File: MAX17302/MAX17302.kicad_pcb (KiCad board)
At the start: 2 copper layers, 20.4 x 50.6 mm, 12 parts, among them J1 Conn_01x02, J2 Conn_01x02, J3 Conn_01x03, Q1 Q_NMOS_DSG, Q2 Q_NMOS_DSG, U1 MAX17302G+T

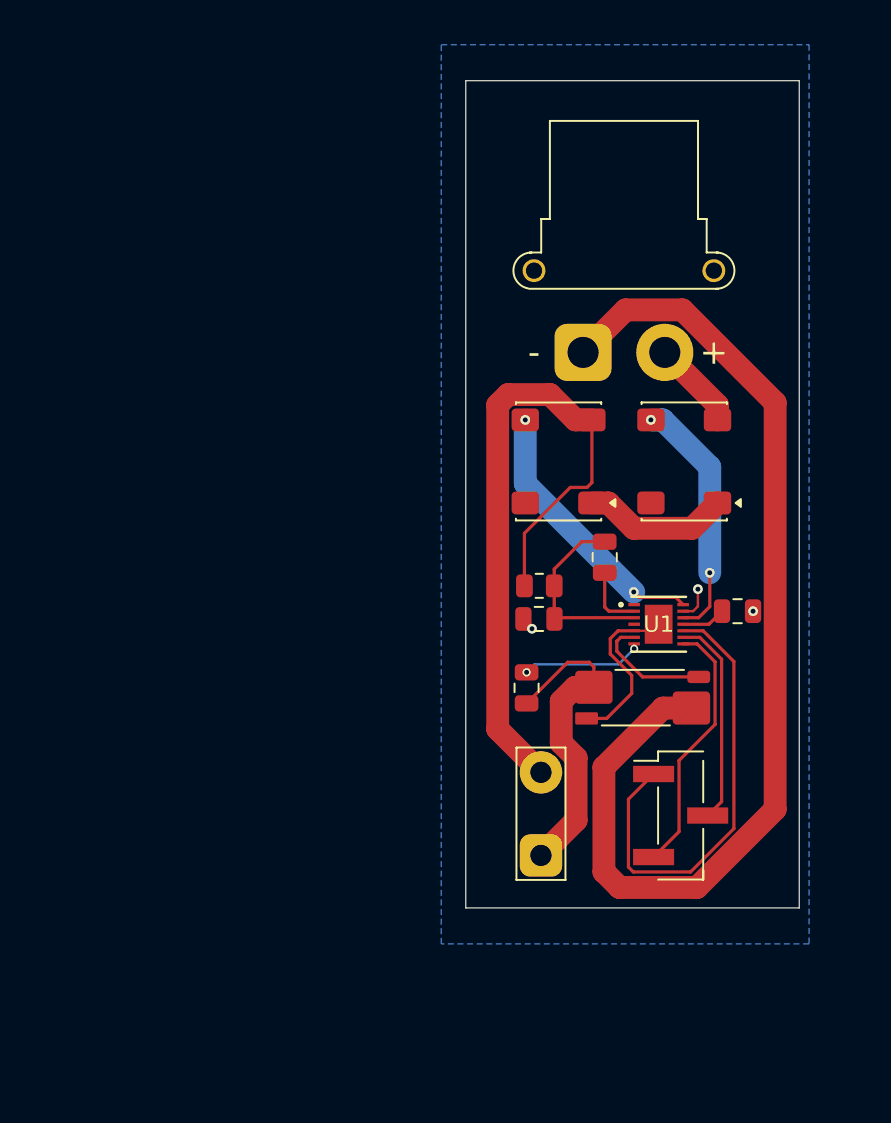
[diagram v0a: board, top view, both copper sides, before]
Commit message: Update PCB layout and add NTC thermistor
- Resolved clearance issues to ensure design safety.
- Adjusted trace widths for better routing.
- Optimized component placements and overall layout.
- Added NTC thermistor for temperature monitoring.
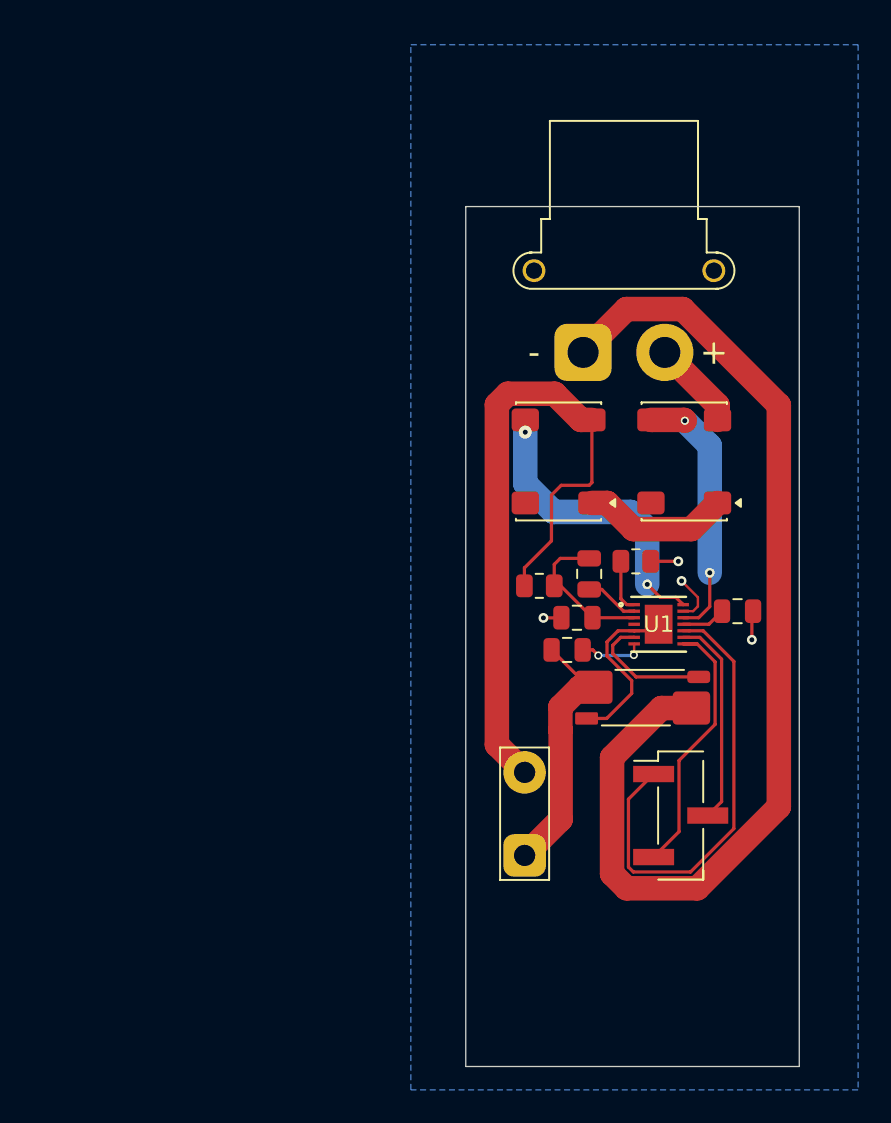
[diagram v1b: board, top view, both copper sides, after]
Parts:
- added TH1: 10kΩ, Resistor_SMD:R_0805_2012Metric, F.Cu at (149.4, 96.6)
- moved C2 3.40 mm to (145.2, 102.0), turned to 180 degrees
- moved C3 2.33 mm to (145.8, 100.0)
- moved C1 1.39 mm to (146.6, 97.4)
- moved J2 1.00 mm to (142.6, 114.6)
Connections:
- U1 pad 1: unconnected-(U1-TH-Pad1) -> Net-(U1-TH)
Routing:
- net GND: track 2.08 -> 7.57 mm, vias 3 -> 4
- net Net-(U1-REG): track 7.48 -> 3.56 mm
- net /CELL-: track 19.6 -> 16.2 mm
- net Net-(U1-TH): track 0.00 -> 3.25 mm
- net /BATT: track 11.7 -> 9.70 mm
- net /CHG: track 16.6 -> 18.0 mm
- net /DIS: track 15.2 -> 16.1 mm
- net Net-(J3-Pin_3): track 15.9 -> 16.7 mm
- net Net-(U1-CP): track 4.00 -> 3.30 mm
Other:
- board size 20.4 x 50.6 mm -> 20.4 x 52.6 mm

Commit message: Rebuild the MAX17302 PCB
also add new 3D of MAX17302
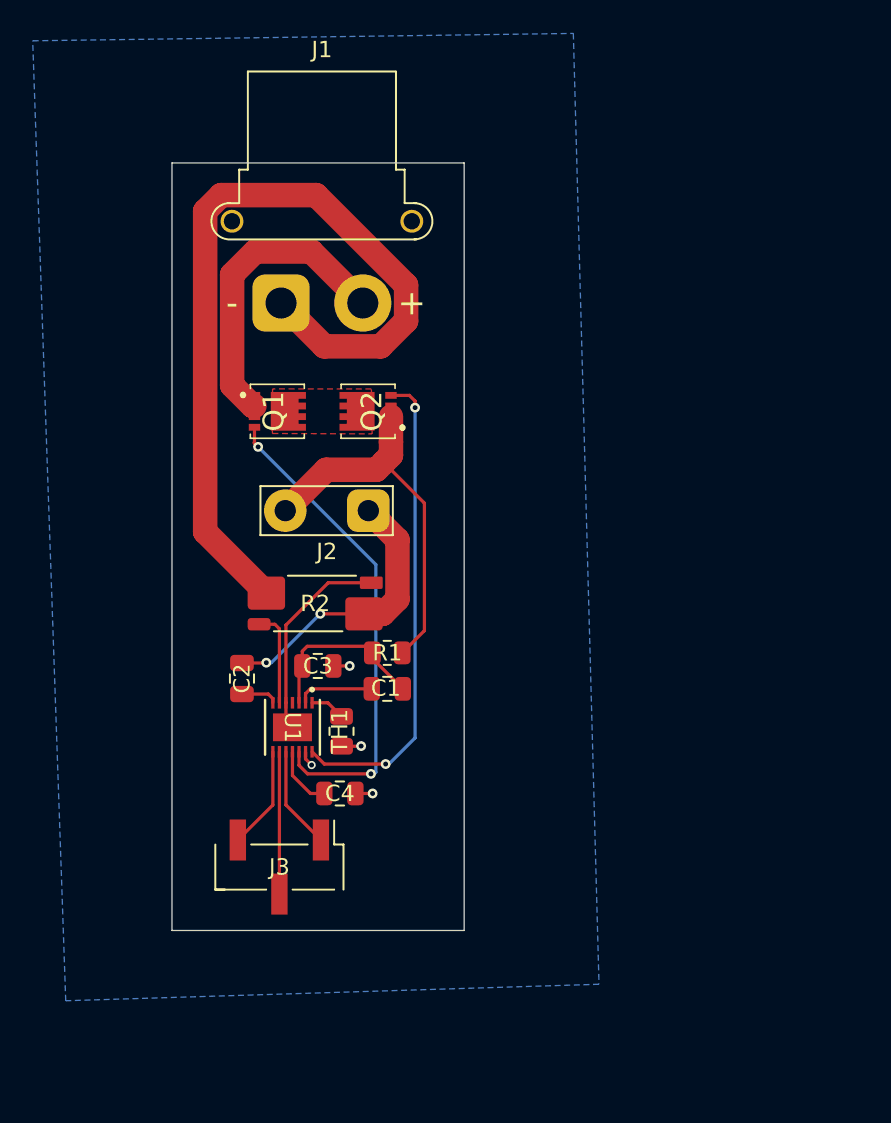
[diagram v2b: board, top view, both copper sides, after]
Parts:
- Q1, Q2: footprint Package_DFN_QFN:DFN-4_5x7mm_P5.08mm -> a:FDMC86139P
- moved C4 26.8 mm to (131.3, 110.8)
- moved Q1 25.5 mm to (127.1, 87.4), turned to -90 degrees
- moved J3 24.7 mm to (127.6, 115.3), turned to -90 degrees
- moved U1 23.3 mm to (128.4, 106.8), turned to -90 degrees
- moved J2 23.2 mm to (133.0, 93.5), turned to 180 degrees
- moved R2 20.8 mm to (129.8, 99.2), turned to 180 degrees
- moved TH1 20.8 mm to (131.4, 107.0), turned to 90 degrees
- moved C2 20.0 mm to (125.3, 103.8), turned to 90 degrees
- moved J1 18.7 mm to (127.7, 80.8)
- moved C3 16.1 mm to (129.9, 103.0), turned to 180 degrees
- moved C1 14.2 mm to (134.2, 104.4), turned to 180 degrees
- moved Q2 11.7 mm to (133.4, 87.4), turned to 90 degrees
- moved R1 10.2 mm to (134.2, 102.2), turned to 0 degrees
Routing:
- net Net-(J3-Pin_1): track 28.1 -> 6.28 mm
- net /CELL+: track 42.8 -> 23.5 mm
- net /PK-: track 65.9 -> 51.5 mm
- net /DIS: track 16.1 -> 30.2 mm
- net /PK+: track 5.47 -> 18.5 mm
- net /CHG: track 18.0 -> 29.5 mm
- net Net-(J3-Pin_3): track 16.7 -> 6.28 mm
- net Net-(Q1-D): track 9.01 -> 0.00 mm
- net Net-(J3-Pin_2): track 12.8 -> 8.71 mm
- net GND: track 7.57 -> 4.22 mm
- net /CSN2: track 7.87 -> 5.88 mm
- net /CSP2: track 10.8 -> 12.7 mm
- net Net-(U1-CP): track 3.30 -> 4.73 mm
- net Net-(U1-REG): track 3.56 -> 2.26 mm, vias 2 -> 0
- net Net-(U1-PCKP): track 2.71 -> 3.86 mm
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- added copper zone on In1.Cu, net GND
- added copper zone on F.Cu, net Net-(Q1-D)
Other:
- board size 20.4 x 52.6 mm -> 17.9 x 47 mm
- copper layers 2 -> 4

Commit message: Add files via upload
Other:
- board size 17.9 x 47 mm -> 17.9 x 46.8 mm
